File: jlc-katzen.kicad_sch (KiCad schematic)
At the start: 9 parts, among them J1 USB_C_Receptacle_USB2.0_16P, U1 RP2040, U2 W25Q128JVS, U3 XC6206PxxxMR, Y1 Crystal

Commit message: draft sch
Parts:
- added C1, C16, C2: 4.7 uF, symbol Device:C
- added C10, C11, C12, C13, C14, C15, C7, C8, C9: 0.1 uF, symbol Device:C
- added C5, C6: 1 uF, symbol Device:C
- added D1: SK9822-2020, badge_custom_parts:LED-SK9822-2020, symbol custom_parts:SK9822-2020
- added J2, J3: Conn_01x04, symbol Connector_Generic:Conn_01x04
- added J4: Conn_01x02, symbol Connector_Generic:Conn_01x02
- added J5: Conn_ARM_SWD_TagConnect_TC2030, Connector:Tag-Connect_TC2030-IDC-FP_2x03_P1.27mm_Vertical, symbol Connector:Conn_ARM_SWD_TagConnect_TC2030
- added Q1, Q2, Q3: 2N7002, Package_TO_SOT_SMD:SOT-23, symbol Transistor_FET:2N7002
- added R1, R2: 5.1k, symbol Device:R
- added R10, R11, R14, R4, R7, R9: 1k, symbol Device:R
- added R12: 200, symbol Device:R
- added R13: 100, symbol Device:R
- added R3, R8: 10k, symbol Device:R
- added R5, R6: 27, symbol Device:R
- C3: renamed from C1; value C_Small -> 18 pF
- C4: renamed from C2; value C_Small -> 18 pF
- Y1: value Crystal -> 12 MHz 20 pF X322512MSB4SI
- renumbered D1 to D2, U3 to U1, U1 to U3
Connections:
- net GND: now also C3.2, C4.2, J1.A1 (GND), J1.A12 (GND), J1.B1 (GND), J1.B12 (GND), J1.S1 (SHIELD), U1.1 (GND), U2.4 (GND), U3.19 (TESTEN), U3.57 (GND), C1.2, C10.2, C11.2, C12.2, C13.2, C14.2, C15.2, C16.2, C2.2, C5.2, C6.2, C7.2, C8.2, C9.2, D1.2 (GND), J2.4 (Pin_4), J3.4 (Pin_4), J4.2 (Pin_2), J5.5 (GND), Q1.2 (S), Q2.2 (S), Q3.2 (S), R1.2, R2.2
- net +5V: now reaches J1.A4 (VBUS), J1.A9 (VBUS), J1.B4 (VBUS), J1.B9 (VBUS)
- net +5V: now also U1.3 (VI), C1.1, D1.5 (VDD), J2.1 (Pin_1), J3.1 (Pin_1), R12.1, R4.1, R9.1
- net CC1: now reaches J1.A5 (CC1)
- net CC1: now also U3.38 (GPIO26_ADC0), R1.1
- net USB_D-: now reaches J1.A6 (D+)
- net USB_D-: now also J1.B6 (D+), R6.1
- net USB_D+: now reaches J1.A7 (D-)
- net USB_D+: now also J1.B7 (D-), R5.1
- net CC2: now reaches J1.B5 (CC2)
- net CC2: now also U3.39 (GPIO27_ADC1), R2.1
- net at U2.1 (~{CS}): now also U3.56 (QSPI_SS), R10.1, R8.2
- net at U2.2 (DO(IO1)): now also U3.55 (QSPI_SD1)
- net at U2.3 (IO2): now also U3.54 (QSPI_SD2)
- net at U2.5 (DI(IO0)): now also U3.53 (QSPI_SD0)
- net at U2.6 (CLK): now also U3.52 (QSPI_SCLK)
- net at U2.7 (IO3): now also U3.51 (QSPI_SD3)
- net +3.3V: now reaches U2.8 (VCC)
- net +3.3V: now also U1.2 (VO), U3.1 (IOVDD), U3.10 (IOVDD), U3.22 (IOVDD), U3.33 (IOVDD), U3.42 (IOVDD), U3.43 (ADC_AVDD), U3.44 (VREG_IN), U3.48 (USB_VDD), U3.49 (IOVDD), C10.1, C11.1, C12.1, C13.1, C14.1, C15.1, C2.1, C5.1, C9.1, J5.1 (VCC), R13.2, R3.1, R8.1
- net at Y1.1: now also C3.1, U3.20 (XIN)
- net at Y1.2: now also C4.1, U3.21 (XOUT)
- net at D2.1 (K): now also Q3.3 (D)
- net at D2.2 (A): now also R12.2
- net PAIR_IN_TX: now reaches U3.2 (GPIO0)
- net PAIR_IN_TX: now also J2.3 (Pin_3)
- net +1V1: now reaches U3.23 (DVDD), U3.50 (DVDD)
- net +1V1: now also U3.45 (VREG_VOUT), C6.1, C7.1, C8.1
- net SWCLK: now reaches U3.24 (SWCLK)
- net SWCLK: now also J5.4 (SWCLK)
- net SWDIO: now reaches U3.25 (SWD)
- net SWDIO: now also J5.2 (SWDIO)
- net ~{RESET}: now reaches U3.26 (RUN)
- net ~{RESET}: now also J5.3 (~{RESET}), R3.2
- net PAIR_IN_RX: now reaches U3.3 (GPIO1)
- net PAIR_IN_RX: now also J2.2 (Pin_2)
- net LED_CLK: now reaches U3.4 (GPIO2)
- net LED_CLK: now also R7.1
- net at U3.46 (USB_DM): now also R6.2
- net at U3.47 (USB_DP): now also R5.2
- net LED_DAT: now reaches U3.5 (GPIO3)
- net LED_DAT: now also R11.1
- net PAIR_OUT_TX: now reaches U3.6 (GPIO4)
- net PAIR_OUT_TX: now also J3.2 (Pin_2)
- net PAIR_OUT_RX: now reaches U3.7 (GPIO5)
- net PAIR_OUT_RX: now also J3.3 (Pin_3)
- net IR_RX: now reaches U3.8 (GPIO6)
- net IR_RX: now also U4.3 (Vout)
- net IR_TX: now reaches U3.9 (GPIO7)
- net IR_TX: now also R14.1
- net at U4.4 (Vcc): now also C16.1, R13.1
- new net: Q3.1 (G), R14.2
- new net: Q1.1 (G), R7.2
- new net: J4.1 (Pin_1), R10.2
- new net: Q2.1 (G), R11.2
- new net LED_CLK_5V: D1.4 (CKI), Q1.3 (D), R4.2
- new net LED_DAT_5V: D1.3 (SDI), Q2.3 (D), R9.2
- no-connect marks 0 -> 3
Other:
- note added: "Decoupling /\ \/"
- note added: "FIGURE OUT HOW MANY FIT ON THE BOARD"
- note added: "RP2040 Vreg"
- note added: "TODO OPTIMIZE PINOUT"
- note added: "Vf = 1 V - 1.5 V assume Vf = 1.25 V target If = 20 mA R = (5 V - 1.25 V) / (20 mA) = 187.5 Ohm -> 200 Ohm is the closest on JLC worst case current -> 17.5 mA"
- moved on the sheet: C3, C4, D2, J1, U1, U2, U3, U4, Y1

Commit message: footprints, part numbers
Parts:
- added C17: 0.1 uF, Capacitor_SMD:C_0402_1005Metric, symbol Device:C
- C1, C2: footprint (none) -> Capacitor_SMD:C_0805_2012Metric; LCSC (none) -> C1779
- C10, C11, C12, C13, C14, C15, C7, C8, C9: footprint (none) -> Capacitor_SMD:C_0402_1005Metric; LCSC (none) -> C1525
- C16: footprint (none) -> Capacitor_SMD:C_0402_1005Metric; LCSC (none) -> C23733
- C3, C4: footprint (none) -> Capacitor_SMD:C_0402_1005Metric; LCSC (none) -> C1549
- C5, C6: footprint (none) -> Capacitor_SMD:C_0603_1608Metric; LCSC (none) -> C15849
- D1: footprint badge_custom_parts:LED-SK9822-2020 -> custom_parts:LED-SK9822-2020; LCSC (none) -> C2909059
- D2: footprint (none) -> LED_SMD:LED_0805_2012Metric; LCSC (none) -> C131250
- J1: footprint (none) -> Connector_USB:USB_C_Receptacle_GCT_USB4105-xx-A_16P_TopMnt_Horizontal; LCSC (none) -> C2765186
- J2, J3: footprint (none) -> Connector_PinHeader_1.27mm:PinHeader_1x04_P1.27mm_Vertical
- J4: footprint (none) -> Connector_PinHeader_1.27mm:PinHeader_1x02_P1.27mm_Vertical
- Q1, Q2, Q3: LCSC (none) -> C7420321
- R1, R2: footprint (none) -> Resistor_SMD:R_0402_1005Metric; LCSC (none) -> C25905
- R10, R11, R14, R4, R7, R9: footprint (none) -> Resistor_SMD:R_0402_1005Metric; LCSC (none) -> C11702
- R12: footprint (none) -> Resistor_SMD:R_0603_1608Metric; LCSC (none) -> C8218
- R13: footprint (none) -> Resistor_SMD:R_0402_1005Metric; LCSC (none) -> C25076
- R3, R8: footprint (none) -> Resistor_SMD:R_0402_1005Metric; LCSC (none) -> C25744
- R5, R6: footprint (none) -> Resistor_SMD:R_0603_1608Metric; LCSC (none) -> C25190
- U1: value XC6206PxxxMR -> XC6206P332MR; LCSC (none) -> C5446
- U2: value W25Q128JVS -> W25Q128JVSIQ; LCSC (none) -> C97521
- U3: LCSC (none) -> C2040
- U4: value ~ -> IRM-H638T/TR2; footprint (none) -> custom_parts:IRM-H6XXT; LCSC (none) -> C91447
- Y1: footprint (none) -> Crystal:Crystal_SMD_3225-4Pin_3.2x2.5mm; LCSC (none) -> C9002
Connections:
- net +3.3V: now also C17.1
- net GND: now also C17.2

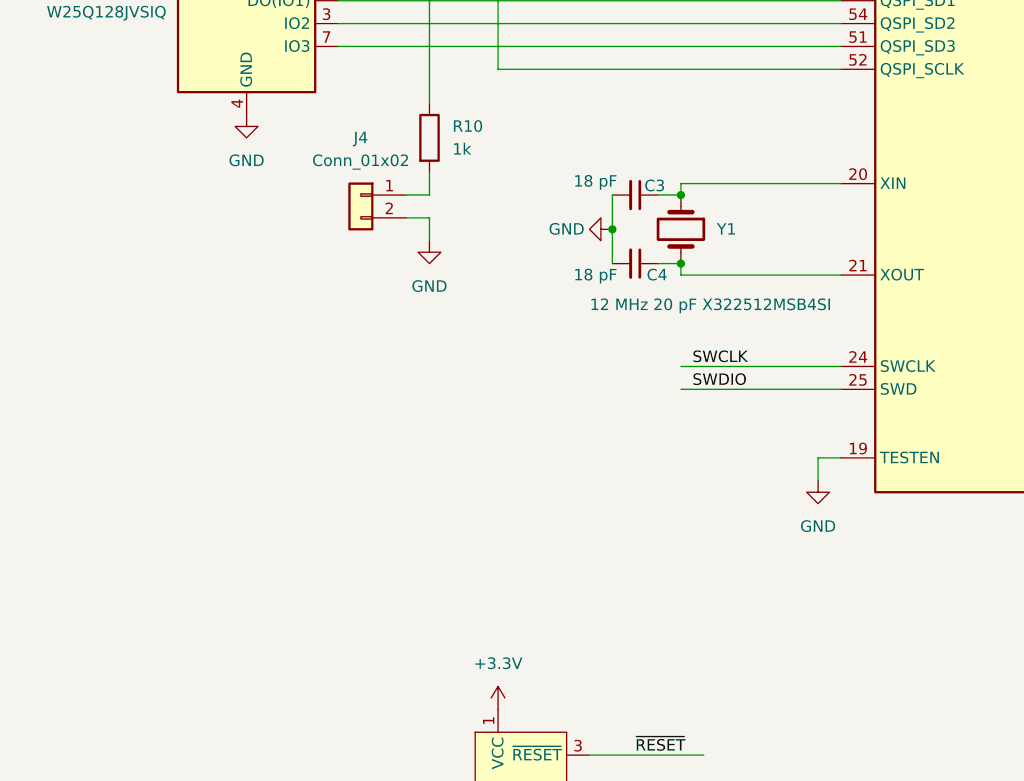
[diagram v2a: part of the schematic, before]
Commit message: fix crystal
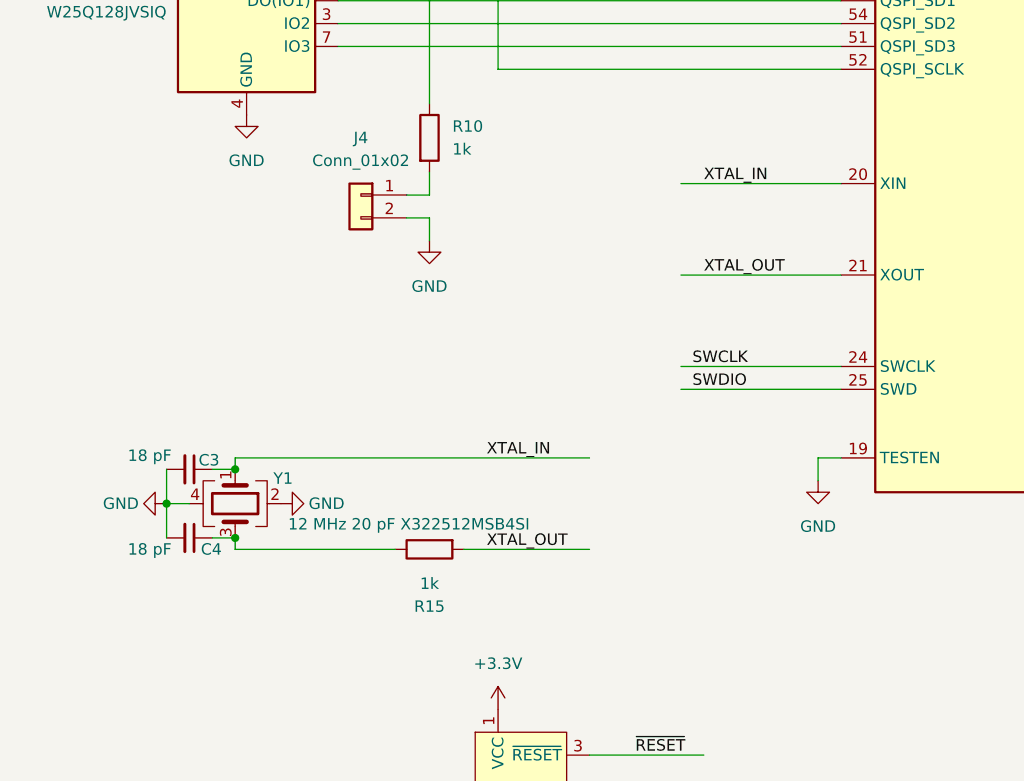
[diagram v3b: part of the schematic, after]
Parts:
- removed Y1: 12 MHz 20 pF X322512MSB4SI, Crystal:Crystal_SMD_3225-4Pin_3.2x2.5mm, symbol Device:Crystal
- added R15: 1k, Resistor_SMD:R_0402_1005Metric, symbol Device:R
- added Y1: 12 MHz 20 pF X322512MSB4SI, Crystal:Crystal_SMD_3225-4Pin_3.2x2.5mm, symbol Device:Crystal_GND24
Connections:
- net GND: now also Y1.2, Y1.4
- net XTAL_IN: now reaches C3.1, U3.20 (XIN)
- net XTAL_IN: now also Y1.1
- net at C4.1: now also R15.1, Y1.3; no longer U3.21 (XOUT)
- new net XTAL_OUT: R15.2, U3.21 (XOUT)
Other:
- moved on the sheet: C3, C4

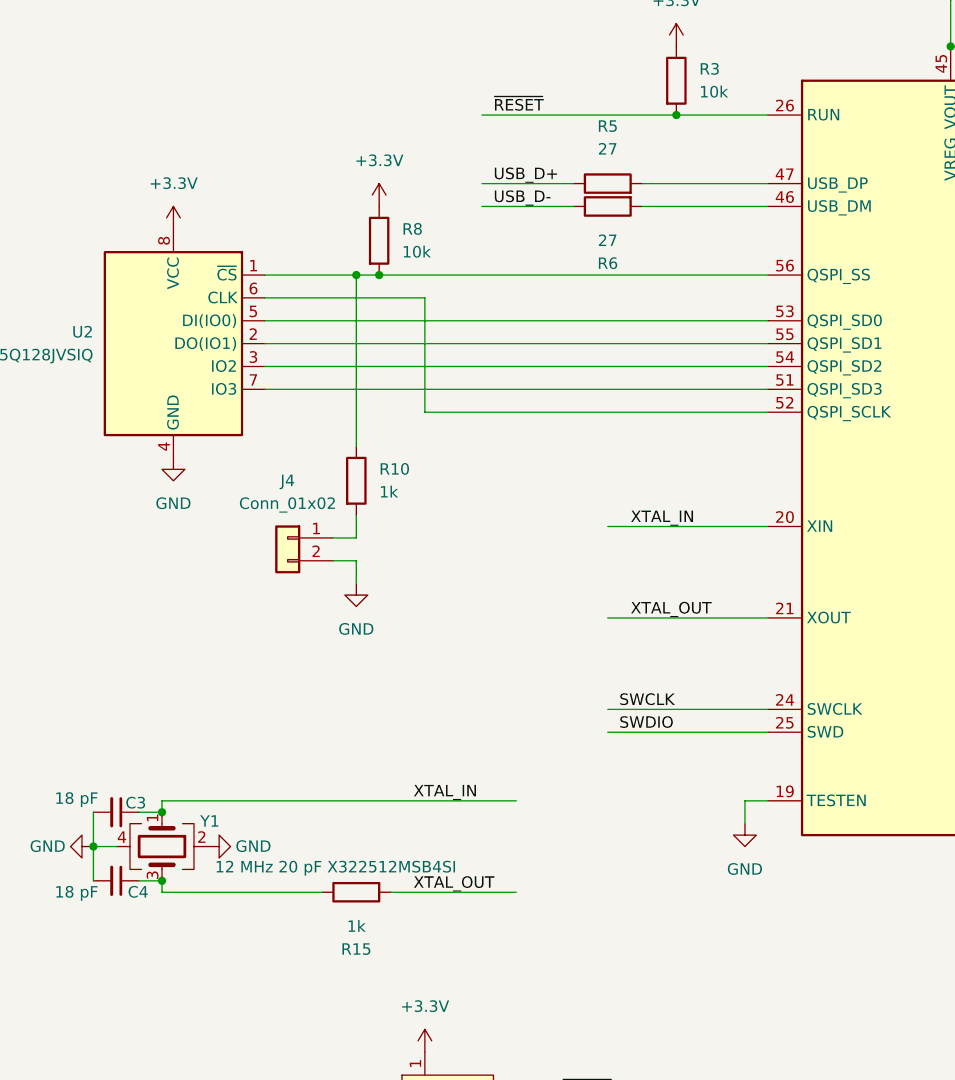
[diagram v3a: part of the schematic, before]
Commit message: name some nets
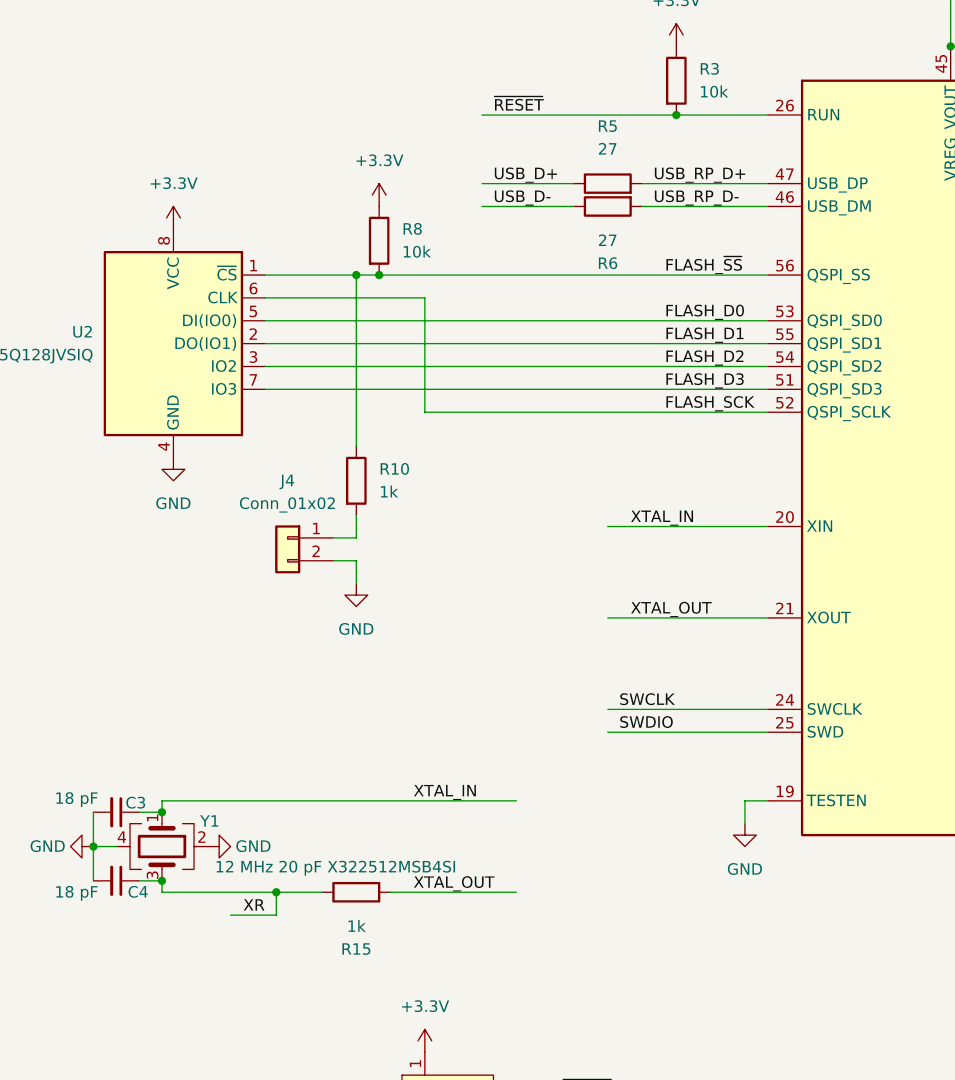
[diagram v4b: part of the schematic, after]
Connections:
- net USB_RP_D-: now reaches R6.2, U3.46 (USB_DM)
- net FLASH_~{SS}: now reaches R10.1, R8.2, U2.1 (~{CS}), U3.56 (QSPI_SS)
- net FLASH_D1: now reaches U2.2 (DO(IO1)), U3.55 (QSPI_SD1)
- net FLASH_D2: now reaches U2.3 (IO2), U3.54 (QSPI_SD2)
- net FLASH_D0: now reaches U2.5 (DI(IO0)), U3.53 (QSPI_SD0)
- net FLASH_SCK: now reaches U2.6 (CLK), U3.52 (QSPI_SCLK)
- net FLASH_D3: now reaches U2.7 (IO3), U3.51 (QSPI_SD3)
- net XR: now reaches C4.1, R15.1, Y1.3
- net USB_RP_D+: now reaches R5.2, U3.47 (USB_DP)
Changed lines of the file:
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@@
+	)
+	(junction
+		(at 46.99 200.66)
+		(diameter 0)
+		(color 0 0 0 0)
 	)
 	(junction
@@
 	(wire
 		(pts
+			(xy 41.91 203.2) (xy 46.99 203.2)
+		)
+		(stroke
+			(width 0)
+			(type default)
+		)
+	)
+	(wire
+		(pts
 			(xy 73.66 228.6) (xy 86.36 228.6)
 		)
@@
 	(wire
 		(pts
-			(xy 34.29 200.66) (xy 52.07 200.66)
+			(xy 34.29 200.66) (xy 46.99 200.66)
 		)
 		(stroke
@@
 	(wire
 		(pts
+			(xy 46.99 200.66) (xy 52.07 200.66)
+		)
+		(stroke
+			(width 0)
+			(type default)
+		)
+	)
+	(wire
+		(pts
 			(xy 298.45 219.71) (xy 313.69 219.71)
 		)
@@
 		(pts
 			(xy 298.45 83.82) (xy 314.96 83.82)
+		)
+		(stroke
+			(width 0)
+			(type default)
+		)
+	)
+	(wire
+		(pts
+			(xy 46.99 200.66) (xy 46.99 203.2)
 		)
 		(stroke
@@
 		)
 	)
+	(label "FLASH_D1"
+		(at 90.17 139.7 0)
+		(fields_autoplaced yes)
+		(effects
+			(font
+				(size 1.27 1.27)
+			)
+			(justify left bottom)
+		)
+	)
+	(label "FLASH_D2"
+		(at 90.17 142.24 0)
+		(fields_autoplaced yes)
+		(effects
+			(font
+				(size 1.27 1.27)
+			)
+			(justify left bottom)
+		)
+	)
+	(label "FLASH_D0"
+		(at 90.17 137.16 0)
+		(fields_autoplaced yes)
+		(effects
+			(font
+				(size 1.27 1.27)
+			)
+			(justify left bottom)
+		)
+	)
 	(label "XTAL_IN"
 		(at 86.36 160.02 0)
@@
 		)
 	)
+	(label "FLASH_D3"
+		(at 90.17 144.78 0)
+		(fields_autoplaced yes)
+		(effects
+			(font
+				(size 1.27 1.27)
+			)
+			(justify left bottom)
+		)
+	)
 	(label "LED_DAT_5V"
 		(at 299.72 81.28 0)
@@
 		)
 	)
+	(label "USB_RP_D+"
+		(at 88.9 121.92 0)
+		(fields_autoplaced yes)
+		(effects
+			(font
+				(size 1.27 1.27)
+			)
+			(justify left bottom)
+		)
+	)
 	(label "PAIR_IN_TX"
 		(at 190.5 57.15 0)
@@
 		)
 	)
+	(label "XR"
+		(at 45.72 203.2 180)
+		(fields_autoplaced yes)
+		(effects
+			(font
+				(size 1.27 1.27)
+			)
+			(justify right bottom)
+		)
+	)
 	(label "USB_D+"
 		(at 67.31 38.1 0)
@@
 		(fields_autoplaced yes)
 		(effects
+			(font
+				(size 1.27 1.27)
+			)
+			(justify left bottom)
+		)
+	)
+	(label "FLASH_~{SS}"
+		(at 90.17 132.08 0)
+		(fields_autoplaced yes)
+		(effects
+			(font
+				(size 1.27 1.27)
+			)
+			(justify left bottom)
+		)
+	)
+	(label "USB_RP_D-"
+		(at 88.9 124.46 0)
+		(fields_autoplaced yes)
+		(effects
+			(font
+				(size 1.27 1.27)
+			)
+			(justify left bottom)
+		)
+	)
+	(label "FLASH_SCK"
+		(at 90.17 147.32 0)
+		(fields_autoplaced yes)
+		(effects
